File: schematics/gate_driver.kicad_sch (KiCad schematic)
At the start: 14 parts, among them T2 P0584NL, U10 VO2611, U11 TC4420

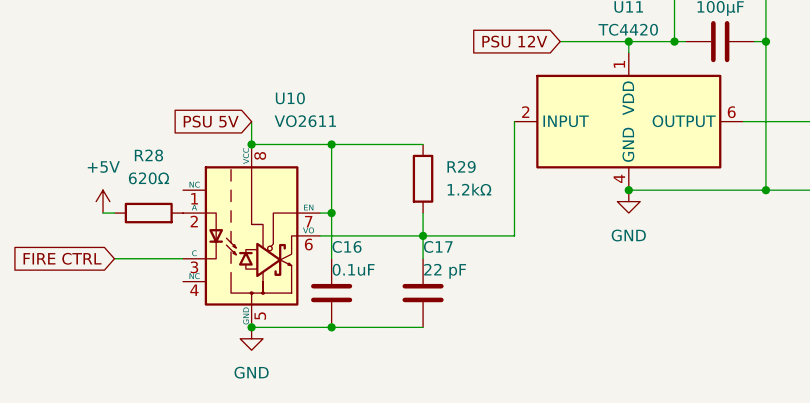
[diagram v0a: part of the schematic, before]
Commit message: Fixed optocoupler wiring bug
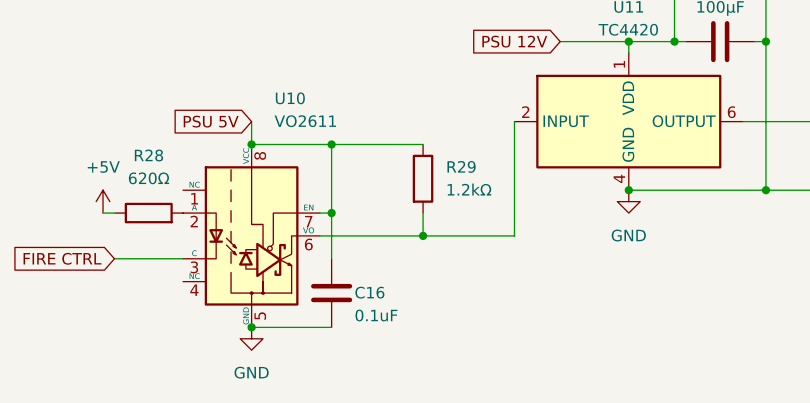
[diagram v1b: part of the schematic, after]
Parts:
- removed C17: 22 pF, symbol Device:C
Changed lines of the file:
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@@
   (junction (at 166.37 93.98) (diameter 0) (color 0 0 0 0)
   )
-  (junction (at 101.6 116.84) (diameter 0) (color 0 0 0 0)
-  )
   (junction (at 101.6 96.52) (diameter 0) (color 0 0 0 0)
   )
@@
     (stroke (width 0) (type default))
   )
-  (wire (pts (xy 101.6 116.84) (xy 111.76 116.84))
-    (stroke (width 0) (type default))
-  )
   (wire (pts (xy 215.9 93.98) (xy 218.44 93.98))
     (stroke (width 0) (type default))
@@
   )
   (wire (pts (xy 76.2 104.14) (xy 77.47 104.14))
-    (stroke (width 0) (type default))
-  )
-  (wire (pts (xy 111.76 106.68) (xy 111.76 109.22))
     (stroke (width 0) (type default))
   )
@@
     )
   )
-  (symbol (lib_id "Device:C") (at 111.76 113.03 0) (unit 1)
-    (in_bom yes) (on_board yes) (dnp no)
-    (property "Reference" "C17" (at 111.76 107.95 0)
-      (effects (font (size 1.27 1.27)) (justify left))
-    )
-    (property "Value" "22 pF" (at 111.76 110.49 0)
-      (effects (font (size 1.27 1.27)) (justify left))
-    )
-    (property "Footprint" "" (at 112.7252 116.84 0)
-      (effects (font (size 1.27 1.27)) hide)
-    )
-    (property "Datasheet" "~" (at 111.76 113.03 0)
-      (effects (font (size 1.27 1.27)) hide)
-    )
-    (pin "1")
-    (pin "2")
-    (instances
-      (project "tms"
-        (path "/dc88686f-c772-4c63-b1cc-83a281c6b46c/025e288f-ab42-4019-86f4-e6a324d46d8a"
-          (reference "C17") (unit 1)
-        )
-      )
-    )
-  )
   (symbol (lib_id "Device:C") (at 144.78 85.09 90) (unit 1)
     (in_bom yes) (on_board yes) (dnp no)
@@
   (symbol (lib_id "Device:C") (at 101.6 113.03 0) (unit 1)
     (in_bom yes) (on_board yes) (dnp no)
-    (property "Reference" "C16" (at 101.6 107.95 0)
-      (effects (font (size 1.27 1.27)) (justify left))
-    )
-    (property "Value" "0.1uF" (at 101.6 110.49 0)
-      (effects (font (size 1.27 1.27)) (justify left))
-    )
+    (property "Reference" "C16" (at 104.14 113.03 0)
+      (effects (font (size 1.27 1.27)) (justify left))
+    )
+    (property "Value" "0.1uF" (at 104.14 115.57 0)
+      (effects (font (size 1.27 1.27)) (justify left))
+    )
